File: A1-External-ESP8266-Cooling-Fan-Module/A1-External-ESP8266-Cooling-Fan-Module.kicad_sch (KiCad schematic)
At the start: 1 part, among them U1 ESP12-F

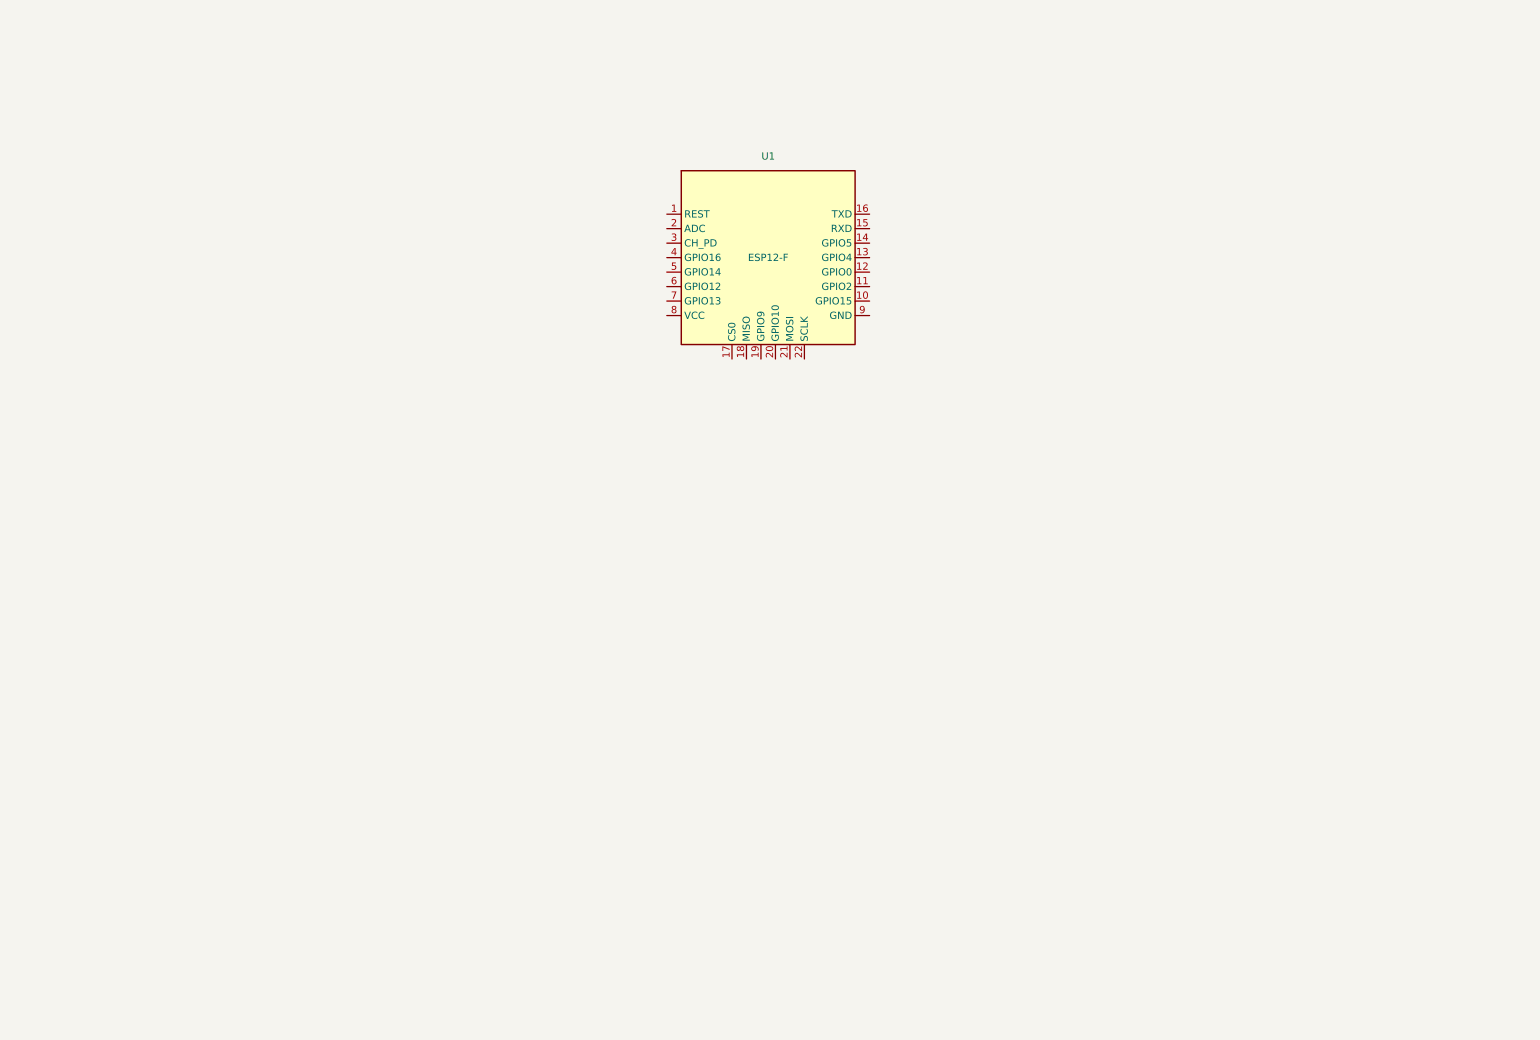
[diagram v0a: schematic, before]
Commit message: USB to UART, Power Supply Circuit
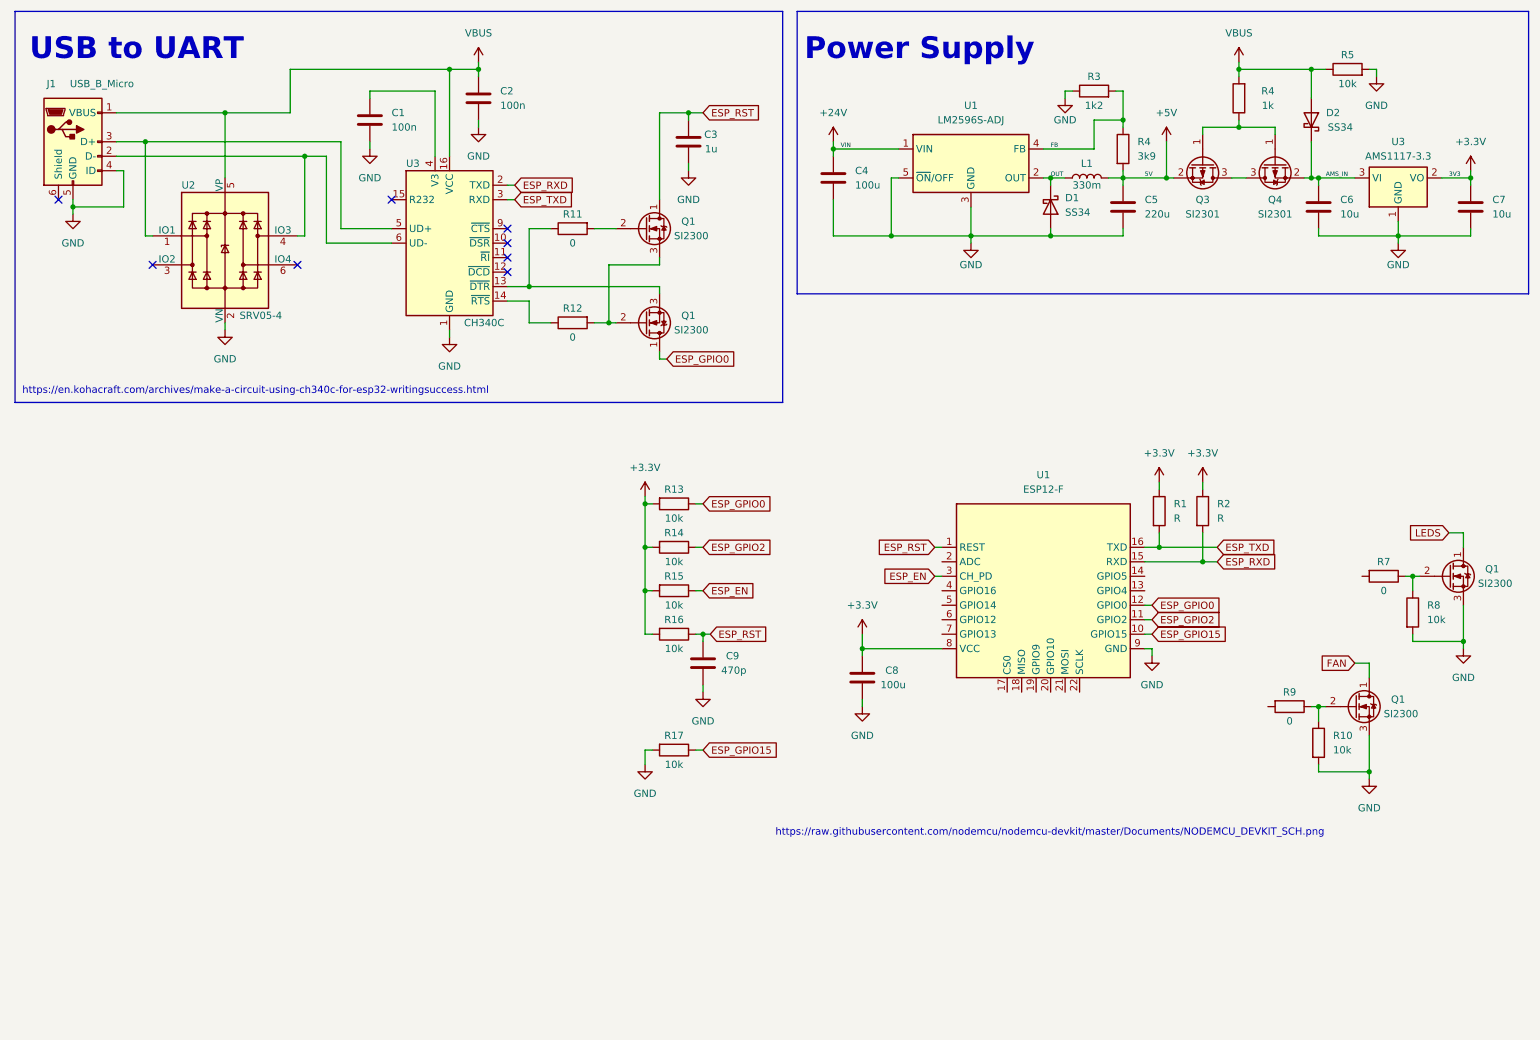
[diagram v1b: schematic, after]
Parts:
- added C1, C2: 100n, Capacitor_SMD:C_0603_1608Metric, symbol Device:C
- added C3: 1u, Capacitor_SMD:C_0603_1608Metric, symbol Device:C
- added C4: 100u, Capacitor_THT:CP_Radial_D8.0mm_P3.80mm, symbol Device:C
- added C5: 220u, Capacitor_SMD:CP_Elec_6.3x7.7, symbol Device:C
- added C6, C7: 10u, Capacitor_SMD:C_0805_2012Metric, symbol Device:C
- added C8: 100u, Capacitor_SMD:C_1206_3216Metric, symbol Device:C
- added C9: 470p, Capacitor_SMD:C_0603_1608Metric, symbol Device:C
- added D1, D2: SS34, Diode_SMD:D_SMA, symbol Device:D_Schottky
- added J1: USB_B_Micro, USB:AMPHENOL_10118194-0001LF, symbol Connector:USB_B_Micro
- added L1: 330m, Inductor_SMD:L_10.4x10.4_H4.8, symbol Device:L
- added Q1 (x4): SI2300, USB:SI2300 SOT-23, symbol Device:Q_NMOS_DGS
- added Q3, Q4: SI2301, Package_TO_SOT_SMD:SOT-23, symbol Device:Q_PMOS_GSD
- added R1, R2: R, Resistor_SMD:R_0603_1608Metric, symbol Device:R
- added R10, R13, R14, R15, R16, R17, R8: 10k, Resistor_SMD:R_0603_1608Metric, symbol Device:R
- added R11, R12, R7, R9: 0, Resistor_SMD:R_0603_1608Metric, symbol Device:R
- added R3: 1k2, Resistor_SMD:R_0603_1608Metric, symbol Device:R
- added R4: 1k, Resistor_SMD:R_0805_2012Metric, symbol Device:R
- added R4: 3k9, Resistor_SMD:R_0603_1608Metric, symbol Device:R
- added R5: 10k, Resistor_SMD:R_0805_2012Metric, symbol Device:R
- added U1: LM2596S-ADJ, Package_TO_SOT_SMD:TO-263-5_TabPin3, symbol Regulator_Switching:LM2596S-ADJ
- added U2: SRV05-4, Package_TO_SOT_SMD:SOT-23-6, symbol Power_Protection:SRV05-4
- added U3: CH340C, Package_SO:SOIC-16_3.9x9.9mm_P1.27mm, symbol Interface_USB:CH340C
- added U3: AMS1117-3.3, Package_TO_SOT_SMD:SOT-223-3_TabPin2, symbol Regulator_Linear:AMS1117-3.3
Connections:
- net ESP_RST: now reaches U1.1 (REST)
- net ESP_RST: now also C3.1, C9.1, Q1.1 (D), R16.1
- net ESP_GPIO15: now reaches U1.10 (GPIO15)
- net ESP_GPIO15: now also R17.1
- net ESP_GPIO2: now reaches U1.11 (GPIO2)
- net ESP_GPIO2: now also R14.1
- net ESP_GPIO0: now reaches U1.12 (GPIO0)
- net ESP_GPIO0: now also Q1.1 (D), R13.1
- net ESP_RXD: now reaches U1.15 (RXD)
- net ESP_RXD: now also R2.2, U3.2 (TXD)
- net ESP_TXD: now reaches U1.16 (TXD)
- net ESP_TXD: now also R1.2, U3.3 (RXD)
- net ESP_EN: now reaches U1.3 (CH_PD)
- net ESP_EN: now also R15.1
- net +3.3V: now reaches U1.8 (VCC)
- net +3.3V: now also C7.1, C8.1, R1.1, R13.2, R14.2, R15.2, R16.2, R2.1, U3.2 (VO)
- net GND: now reaches U1.9 (GND)
- net GND: now also C1.2, C2.2, C3.2, C4.2, C5.2, C6.2, C7.2, C8.2, C9.2, D1.2 (A), J1.4 (ID), J1.5 (GND), Q1.3 (S), Q1.3 (S), R10.2, R17.2, R3.1, R5.2, R8.2, U1.3 (GND), U1.5 (~{ON}/OFF), U2.2 (VN), U3.1 (GND), U3.1 (GND)
- new net: Q1.2 (G), R11.2
- new net: Q1.2 (G), Q1.3 (S), R12.2
- new net: Q3.1 (G), Q4.1 (G), R4.1
- new net: Q3.3 (D), Q4.3 (D)
- new net: R12.1, U3.14 (~{RTS})
- new net: Q1.3 (S), R11.1, U3.13 (~{DTR})
- new net: C1.1, U3.4 (V3)
- new net: J1.3 (D+), U2.1 (IO1), U3.5 (UD+)
- new net: J1.2 (D-), U2.4 (IO3), U3.6 (UD-)
- new net: Q1.2 (G), R7.1, R8.1
- new net: Q1.2 (G), R10.1, R9.1
- new net +24V: C4.1, U1.1 (VIN)
- new net +5V: C5.1, L1.2, Q3.2 (S), R4.2
- new net AMS_IN: C6.1, D2.1 (K), Q4.2 (S), U3.3 (VI)
- new net FAN: Q1.1 (D)
- new net FB: R3.2, R4.1, U1.4 (FB)
- new net LEDS: Q1.1 (D)
- new net OUT: D1.1 (K), L1.1, U1.2 (OUT)
- new net VBUS: C2.1, D2.2 (A), J1.1 (VBUS), R4.2, R5.1, U2.5 (VP), U3.16 (VCC)
- no-connect marks 0 -> 8
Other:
- note added: "Power Supply"
- note added: "USB to UART"
- note added: "https://en.kohacraft.com/archives/make-a-circuit-using-ch340c-for-esp32-writingsuccess.html"
- note added: "https://raw.githubusercontent.com/nodemcu/nodemcu-devkit/master/Documents/NODEMCU_DEVKIT_SCH.png"
- moved on the sheet: U1

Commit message: fixed 3.3v to ch340 chip
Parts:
- removed C2: 100n, Capacitor_SMD:C_0603_1608Metric, symbol Device:C
- added F1: 1A5, Fuse:Fuse_1206_3216Metric, symbol Device:Fuse
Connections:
- net +3.3V: now also C1.1, U3.16 (VCC), U3.4 (V3)
- net ESP_EN: now also C3.1, Q1.1 (D)
- net ESP_RST: no longer C3.1, Q1.1 (D)
- net VBUS: now also F1.2; no longer J1.1 (VBUS), U3.16 (VCC)
- new net: F1.1, J1.1 (VBUS)
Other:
- moved on the sheet: C1

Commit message: finished schematic?
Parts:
- removed C8: 100u, Capacitor_SMD:C_1206_3216Metric, symbol Device:C
- added C2: 100u, Capacitor_SMD:C_1206_3216Metric, symbol Device:C
- added D3: 1N4148, Diode_SMD:D_SOD-123, symbol Diode:1N4148
- added J2: Fan connector, Connector_JST:JST_PH_B2B-PH-K_1x02_P2.00mm_Vertical, symbol Connector_Generic:Conn_01x02
- added J4: PIR sensor, symbol Connector_Generic:Conn_01x03
- added J7: Leds connector, Connector_JST:JST_PH_B2B-PH-K_1x02_P2.00mm_Vertical, symbol Connector_Generic:Conn_01x02
- added JP1: SolderJumper_3_Open, Jumper:SolderJumper-3_P1.3mm_Open_RoundedPad1.0x1.5mm, symbol Jumper:SolderJumper_3_Open
- added R18, R19: 4k7, Resistor_SMD:R_0603_1608Metric, symbol Device:R
- added U6: AM2320, Custom:AM2320, symbol New_Library:AM2320
- R1, R2: value R -> 4k7
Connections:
- net AMS_IN is gone; now on net +5V: C6.1, D2.1 (K), Q4.2 (S), U3.3 (VI)
- net +24V: now also D3.1 (K), J2.1 (Pin_1), J7.1 (Pin_1)
- net +3.3V: now also C2.1, JP1.3 (B), R18.1, R19.1, U6.1 (VDD)
- net +5V: now also JP1.1 (A); no longer C5.1, L1.2, Q3.2 (S), R4.2
- net ESP_RXD: now also R1.2; no longer R2.2
- net ESP_TXD: now also R2.2; no longer R1.2
- net GND: now also C2.2, J4.3 (Pin_3), U6.3 (GND)
- net D+: now reaches J1.3 (D+), U2.1 (IO1), U3.5 (UD+)
- net D-: now reaches J1.2 (D-), U3.6 (UD-)
- net D-: now also U2.6 (IO4); no longer U2.4 (IO3)
- net at U1.13 (GPIO4): now also R19.2, U6.2 (SDA)
- net at U1.14 (GPIO5): now also R18.2, U6.4 (SCL)
- net ESP_PIR-SENS: now reaches U1.5 (GPIO14)
- net ESP_PIR-SENS: now also J4.2 (Pin_2)
- net ESP_PWM-LEDS: now reaches U1.6 (GPIO12)
- net ESP_PWM-LEDS: now also R7.2
- net ESP_PWM-FAN: now reaches U1.7 (GPIO13)
- net ESP_PWM-FAN: now also R9.2
- net FAN: no longer names the net of Q1.1 (D)
- net FAN: now also D3.2 (A), J2.2 (Pin_2)
- net LEDS: no longer names the net of Q1.1 (D)
- net LEDS: now also J7.2 (Pin_2)
- new net: C5.1, L1.2, Q3.2 (S), R4.2
- new net: J4.1 (Pin_1), JP1.2 (C)
- no-connect marks 8 -> 16
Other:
- note added: "ESP12-F, Sensor Connectors"
- note added: "PIR sensor has its own 3V3 regualtor"
- note added: "Temp & Humidity sensor"
- company: (none) -> nissinja
- moved on the sheet: C3, C9, D2, F1, Q1, R10, R13, R14, R15, R16, R17, R7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

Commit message: final layout
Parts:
- added C10, C8: 100n, Capacitor_SMD:C_0603_1608Metric, symbol Device:C
- added D10, D4, D5, D6, D7, D8, D9: LED, LED_SMD:LED_0805_2012Metric, symbol Device:LED
- added H1, H2, H3: MountingHole, MountingHole:MountingHole_3.2mm_M3_DIN965_Pad, symbol Mechanical:MountingHole
- added J5: 24V IN, Connector_JST:JST_PH_B2B-PH-K_1x02_P2.00mm_Vertical, symbol Connector_Generic:Conn_01x02
- added J6, J8: 3V3 OUT, Connector_JST:JST_PH_B2B-PH-K_1x02_P2.00mm_Vertical, symbol Connector_Generic:Conn_01x02
- added J7: LEDS, Connector_PinHeader_2.54mm:PinHeader_2x03_P2.54mm_Vertical, symbol Connector_Generic:Conn_02x03_Odd_Even
- added JP2: Cutoff bypass, Jumper:SolderJumper-2_P1.3mm_Open_RoundedPad1.0x1.5mm, symbol Jumper:SolderJumper_2_Open
- added R20: 2k2, Resistor_SMD:R_0603_1608Metric, symbol Device:R
- added R21: 130, Resistor_SMD:R_0603_1608Metric, symbol Device:R
- added R22: 300, Resistor_SMD:R_0603_1608Metric, symbol Device:R
- added R23, R24, R25, R26, R27: 0, Resistor_SMD:R_0603_1608Metric, symbol Device:R
- C2: footprint Capacitor_SMD:C_1206_3216Metric -> Capacitor_SMD:CP_Elec_6.3x7.7
- C4: footprint Capacitor_THT:CP_Radial_D8.0mm_P3.80mm -> Capacitor_SMD:CP_Elec_8x10.5
- C5: footprint Capacitor_SMD:CP_Elec_6.3x7.7 -> Capacitor_SMD:CP_Elec_10x10.5
- J4: footprint (none) -> Connector_JST:JST_PH_B3B-PH-K_1x03_P2.00mm_Vertical
- R1, R18, R19, R2: value 4k7 -> 1k
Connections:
- net +24V: now also J5.1 (Pin_1), J7.2 (Pin_2)
- net +3.3V: now also C8.1, D10.2 (A), D7.2 (A), D8.2 (A), D9.2 (A), J6.1 (Pin_1), J7.4 (Pin_4), J8.1 (Pin_1); no longer R1.1, R18.1, R19.1, R2.1
- net +5V: now also J7.6 (Pin_6), JP2.2 (B)
- net ESP_PIR-SENS: now also R27.2; no longer J4.2 (Pin_2)
- net ESP_PWM-FAN: now also U1.13 (GPIO4); no longer U1.7 (GPIO13)
- net ESP_PWM-LEDS: now also U1.14 (GPIO5); no longer U1.6 (GPIO12)
- net ESP_RXD: now also R24.1; no longer U1.15 (RXD)
- net ESP_TXD: now also R23.1; no longer U1.16 (TXD)
- net GND: now also C10.2, C8.2, D4.1 (K), D5.1 (K), D6.1 (K), J5.2 (Pin_2), J6.2 (Pin_2), J8.2 (Pin_2)
- net at Q1.2 (G), R12.2: no longer Q1.3 (S)
- net LM2596-OUT: now reaches C5.1, L1.2, Q3.2 (S), R4.2
- net LM2596-OUT: now also JP2.1 (A)
- net at R12.1, U3.14 (~{RTS}): now also Q1.3 (S)
- net at R19.2, U6.2 (SDA): now also R26.2; no longer U1.13 (GPIO4)
- net at R18.2, U6.4 (SCL): now also R25.2; no longer U1.14 (GPIO5)
- new net: J7.3 (Pin_3), R21.1
- new net: D5.2 (A), R21.2
- new net: J7.5 (Pin_5), R22.1
- new net: D6.2 (A), R22.2
- new net: D7.1 (K), R19.1
- new net: D9.1 (K), R1.1
- new net: R24.2, U1.15 (RXD)
- new net: R23.2, U1.16 (TXD)
- new net: D8.1 (K), R18.1
- new net: J7.1 (Pin_1), R20.1
- new net: D10.1 (K), R2.1
- new net: C10.1, J4.2 (Pin_2), R27.1
- new net: D4.2 (A), R20.2
- new net SCL: R25.1, U1.6 (GPIO12)
- new net SDA: R26.1, U1.7 (GPIO13)
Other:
- note added: "Approx 10mA"
- moved on the sheet: C4, C5, C6, C7, C9, D1, D2, D3, J2, J4, J7, JP1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
